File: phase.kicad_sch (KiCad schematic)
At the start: 4 parts

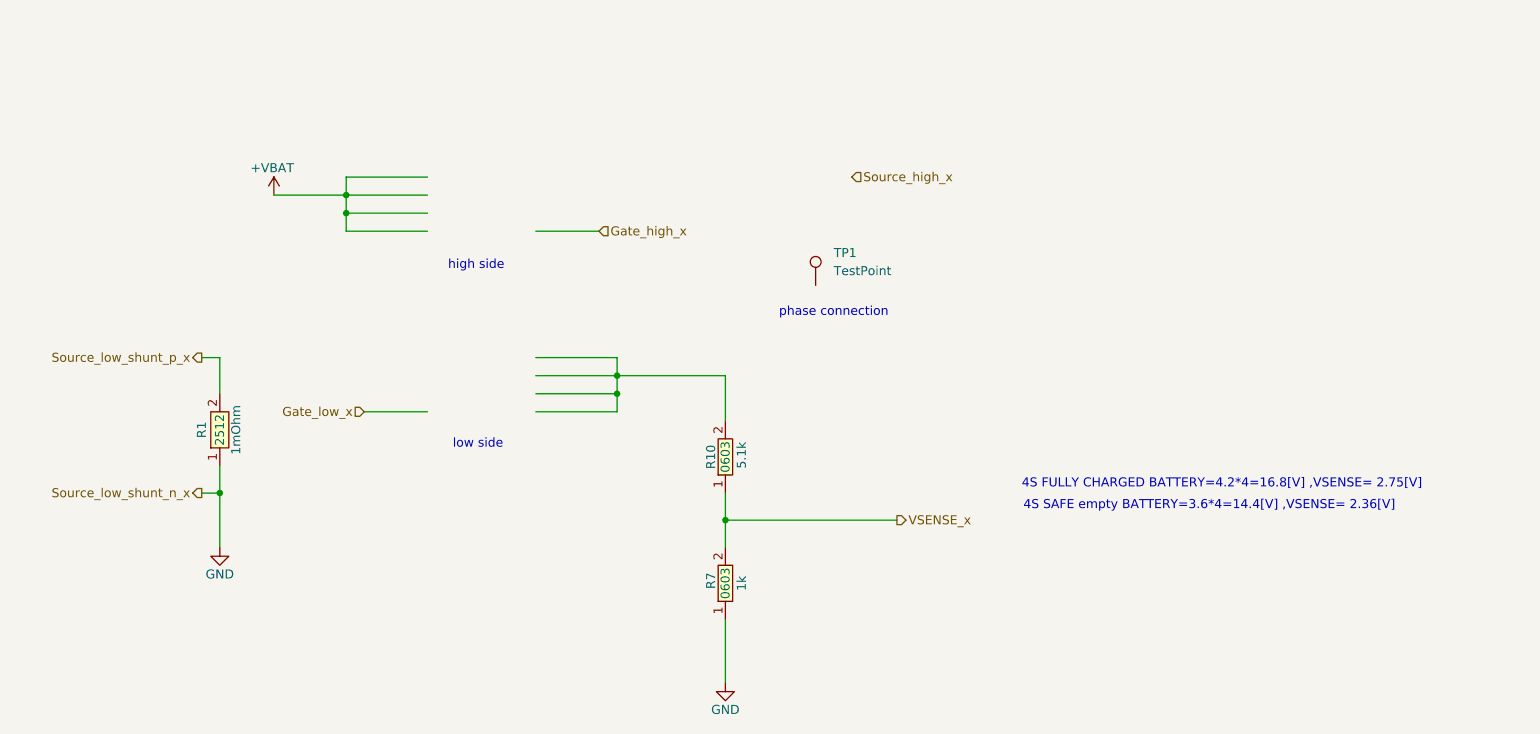
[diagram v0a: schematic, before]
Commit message: Finished power and phase blocks
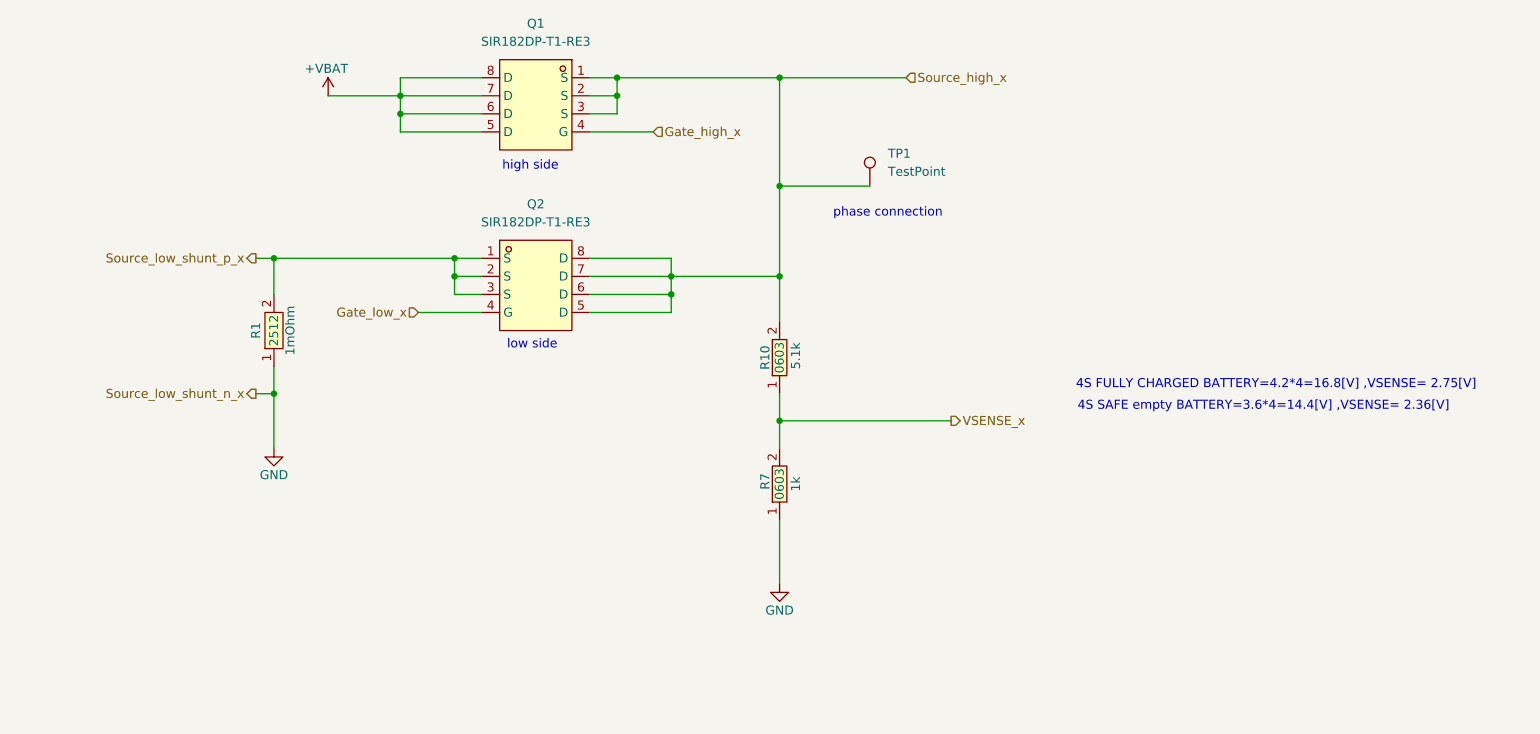
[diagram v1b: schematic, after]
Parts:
- added Q1, Q2: SIR182DP-T1-RE3, easyeda2kicad:POWERPAK-SO-8_L5.9-W4.9-P1.27-LS6.2-BL, symbol easyeda_symbole:SIR182DP-T1-RE3
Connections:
- net +VBAT: now also Q1.5 (D), Q1.6 (D), Q1.7 (D), Q1.8 (D)
- net Gate_high_x: now also Q1.4 (G)
- net Gate_low_x: now also Q2.4 (G)
- net Source_high_x: now also R10.2, TP1.1, Q1.1 (S), Q1.2 (S), Q1.3 (S), Q2.5 (D), Q2.6 (D), Q2.7 (D), Q2.8 (D)
- net Source_low_shunt_p_x: now also Q2.1 (S), Q2.2 (S), Q2.3 (S)
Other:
- moved on the sheet: R1, R10, R7, TP1
